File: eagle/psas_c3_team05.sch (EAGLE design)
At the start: 92 parts, among them IC1 CP2102, J1 3220-10-0100-00, J2 1.27MM_HDR_2X12X1, U1 MIC5319 3.3V, U2 MCP73871, U3 MKW01Z128, X1 32 MHz

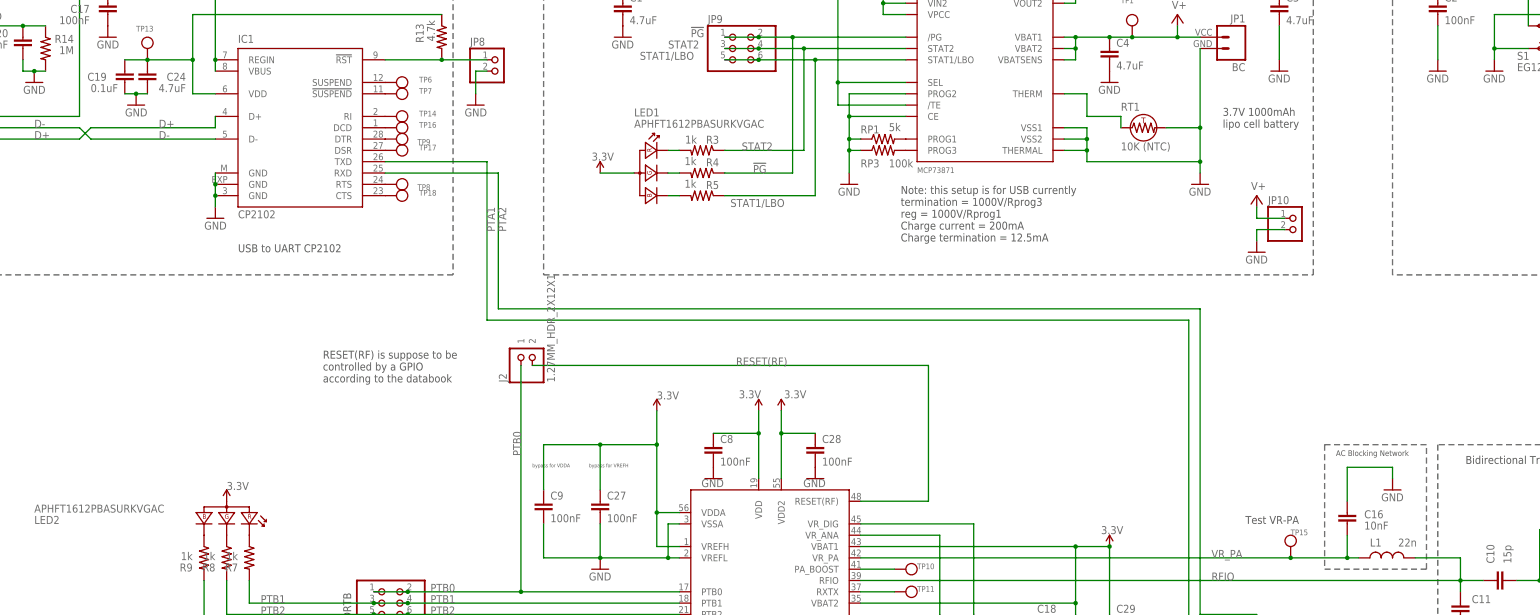
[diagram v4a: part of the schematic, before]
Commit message: I added a few more parts
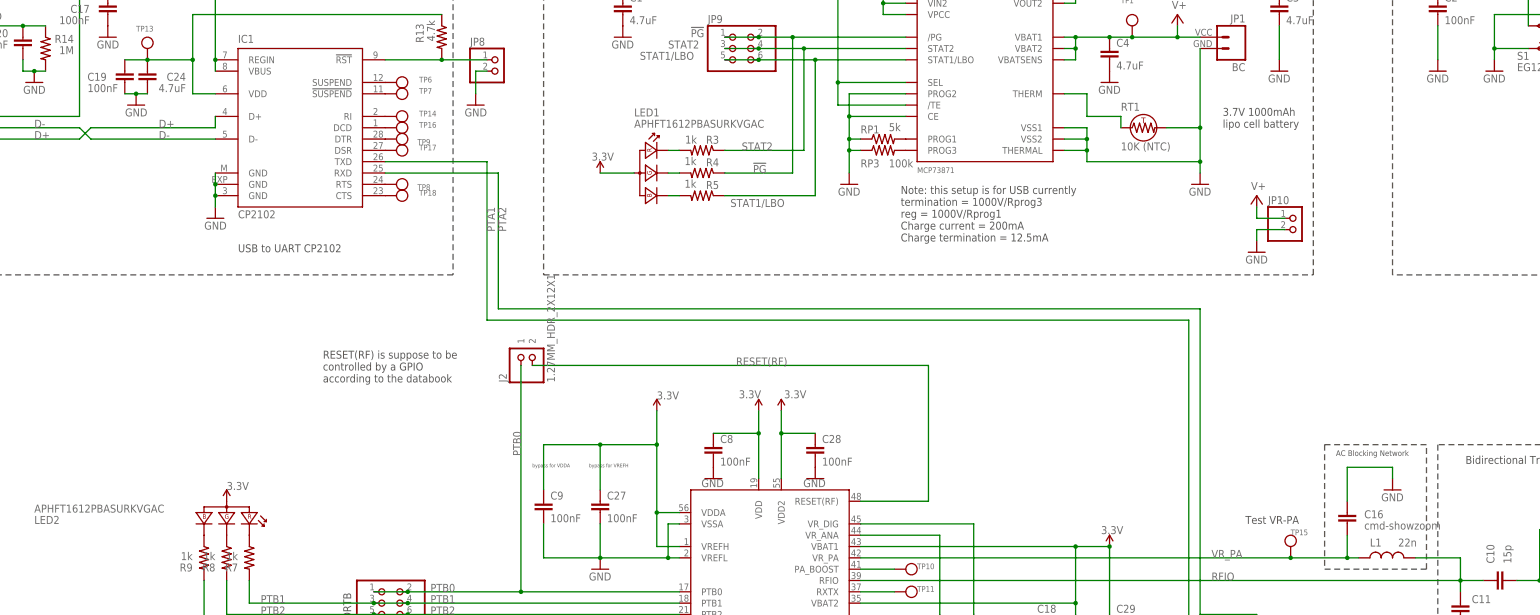
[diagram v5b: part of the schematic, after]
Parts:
- C15: DPN (none) -> 490-1532-1-ND
- C16: value 10nF -> cmd-showzoom
- C19: value 0.1uF -> 100nF
- C2, C5, C7: DPN (none) -> 490-1532-1-ND; DSN 490-1532-1-ND -> (none)
- C6: DPN (none) -> 490-3906-1-ND
- LED1, LED2: DPN 160-2022-1-ND -> 754-1100-1-ND
- LED3: DPN (none) -> 160-1446-1-ND
- R2: DPN (none) -> 311-1.00KHRCT-ND
- S1: DPN (none) -> EG1903-ND; DSN EG1903-ND -> (none)
- X1: DPN (none) -> SER3672CT-ND
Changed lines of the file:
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@@
 <part name="TP1" library="microbuilder" deviceset="TESTPOINT" device="ROUND0.5MM"/>
 <part name="C2" library="rcl_custom" deviceset="C-EU" device="0603-B-NOSILK" value="100nF">
-<attribute name="DSN" value="490-1532-1-ND"/>
+<attribute name="DPN" value="490-1532-1-ND"/>
 </part>
 <part name="GND4" library="Vibrogait_prototype" deviceset="GND" device=""/>
@@
 <part name="TP3" library="microbuilder" deviceset="TESTPOINT" device="ROUND0.5MM"/>
 <part name="C5" library="rcl_custom" deviceset="C-EU" device="0603-B-NOSILK" value="100nF">
-<attribute name="DSN" value="490-1532-1-ND"/>
-</part>
-<part name="C6" library="rcl_custom" deviceset="C-EU" device="0805-B-NOSILK" value="2.2uF"/>
+<attribute name="DPN" value="490-1532-1-ND"/>
+</part>
+<part name="C6" library="rcl_custom" deviceset="C-EU" device="0805-B-NOSILK" value="2.2uF">
+<attribute name="DPN" value="490-3906-1-ND"/>
+</part>
 <part name="C7" library="rcl_custom" deviceset="C-EU" device="0603-B-NOSILK" value="100nF">
-<attribute name="DSN" value="490-1532-1-ND"/>
+<attribute name="DPN" value="490-1532-1-ND"/>
 </part>
 <part name="GND7" library="Vibrogait_prototype" deviceset="GND" device=""/>
@@
 <part name="GND10" library="Vibrogait_prototype" deviceset="GND" device=""/>
 <part name="S1" library="Vibrogait_prototype" deviceset="SWITCH-SPST" device="PTH" value="EG1218">
-<attribute name="DSN" value="EG1903-ND"/>
+<attribute name="DPN" value="EG1903-ND"/>
 </part>
 <part name="GND11" library="Vibrogait_prototype" deviceset="GND" device=""/>
@@
 <part name="GND18" library="Vibrogait_prototype" deviceset="GND" device=""/>
 <part name="GND19" library="Vibrogait_prototype" deviceset="GND" device=""/>
-<part name="C15" library="rcl_custom" deviceset="C-EU" device="0603-B-NOSILK" value="100nF"/>
-<part name="C16" library="rcl_custom" deviceset="C-EU" device="0603-B-NOSILK" value="10nF"/>
+<part name="C15" library="rcl_custom" deviceset="C-EU" device="0603-B-NOSILK" value="100nF">
+<attribute name="DPN" value="490-1532-1-ND"/>
+</part>
+<part name="C16" library="rcl_custom" deviceset="C-EU" device="0603-B-NOSILK" value="cmd-showzoom"/>
 <part name="GND20" library="Vibrogait_prototype" deviceset="GND" device=""/>
 <part name="L1" library="rcl_custom" deviceset="L-US" device="0603-B-NOSILK" value="22n"/>
@@
 <attribute name="DPN" value="490-1532-1-ND"/>
 </part>
-<part name="C19" library="rcl_custom" deviceset="C-EU" device="0603-B-NOSILK" value="0.1uF">
+<part name="C19" library="rcl_custom" deviceset="C-EU" device="0603-B-NOSILK" value="100nF">
 <attribute name="DIST" value="Digi-Key"/>
 <attribute name="DPN" value="490-1532-1-ND"/>
@@
 <part name="GND25" library="Vibrogait_prototype" deviceset="GND" device=""/>
 <part name="LED1" library="Vibrogait_prototype" deviceset="LED_RGB_COMMON_ANODE-*" device="1.6X1.26" value="APHFT1612PBASURKVGAC">
-<attribute name="DPN" value="160-2022-1-ND"/>
+<attribute name="DPN" value="754-1100-1-ND"/>
 </part>
 <part name="R3" library="rcl_custom" deviceset="R-US_" device="0603-B-NOSILK" value="1k">
@@
 <part name="C21" library="rcl_custom" deviceset="C-EU" device="0603-B-NOSILK" value="1nF"/>
 <part name="GND27" library="Vibrogait_prototype" deviceset="GND" device=""/>
-<part name="X1" library="crystal" deviceset="FC-12M" device="" value="32 MHz"/>
+<part name="X1" library="crystal" deviceset="FC-12M" device="" value="32 MHz">
+<attribute name="DPN" value="SER3672CT-ND"/>
+</part>
 <part name="R6" library="rcl_custom" deviceset="R-US_" device="0603-B-NOSILK" value="0"/>
 <part name="C22" library="Vibrogait_prototype" deviceset="C-EU" device="0603-B-NOSILK" value="11pF">
@@
 <part name="TP18" library="microbuilder" deviceset="TESTPOINT" device="ROUND0.5MM"/>
 <part name="LED2" library="Vibrogait_prototype" deviceset="LED_RGB_COMMON_ANODE-*" device="1.6X1.26" value="APHFT1612PBASURKVGAC">
-<attribute name="DPN" value="160-2022-1-ND"/>
-</part>
-<part name="LED3" library="Vibrogait_prototype" deviceset="LED" device="-0603" value="GRN"/>
-<part name="R2" library="rcl_custom" deviceset="R-US_" device="0603-B-NOSILK" value="1k"/>
+<attribute name="DPN" value="754-1100-1-ND"/>
+</part>
+<part name="LED3" library="Vibrogait_prototype" deviceset="LED" device="-0603" value="GRN">
+<attribute name="DPN" value="160-1446-1-ND"/>
+</part>
+<part name="R2" library="rcl_custom" deviceset="R-US_" device="0603-B-NOSILK" value="1k">
+<attribute name="DPN" value="311-1.00KHRCT-ND"/>
+</part>
 <part name="GND38" library="Vibrogait_prototype" deviceset="GND" device=""/>
 <part name="R7" library="rcl_custom" deviceset="R-US_" device="0603-B-NOSILK" value="1k"/>
@@
 <attribute name="NAME" x="392.684" y="348.361" size="1.778" layer="95"/>
 <attribute name="VALUE" x="392.684" y="343.281" size="1.778" layer="96"/>
-<attribute name="DSN" x="391.16" y="347.98" size="1.778" layer="96" display="off"/>
+<attribute name="DPN" x="391.16" y="347.98" size="1.778" layer="96" display="off"/>
 </instance>
 <instance part="GND4" gate="1" x="391.16" y="332.74" smashed="yes">
@@
 <attribute name="NAME" x="451.104" y="345.821" size="1.778" layer="95"/>
 <attribute name="VALUE" x="451.104" y="340.741" size="1.778" layer="96"/>
-<attribute name="DSN" x="449.58" y="345.44" size="1.778" layer="96" display="off"/>
+<attribute name="DPN" x="449.58" y="345.44" size="1.778" layer="96" display="off"/>
 </instance>
 <instance part="C6" gate="CE" x="464.82" y="345.44" smashed="yes">
 <attribute name="NAME" x="466.344" y="345.821" size="1.778" layer="95"/>
 <attribute name="VALUE" x="466.344" y="340.741" size="1.778" layer="96"/>
+<attribute name="DPN" x="464.82" y="345.44" size="1.778" layer="96" display="off"/>
 </instance>
 <instance part="C7" gate="CE" x="439.42" y="337.82" smashed="yes">
 <attribute name="NAME" x="440.944" y="338.201" size="1.778" layer="95"/>
 <attribute name="VALUE" x="440.944" y="333.121" size="1.778" layer="96"/>
-<attribute name="DSN" x="439.42" y="337.82" size="1.778" layer="96" display="off"/>
+<attribute name="DPN" x="439.42" y="337.82" size="1.778" layer="96" display="off"/>
 </instance>
 <instance part="GND7" gate="1" x="439.42" y="327.66" smashed="yes">
@@
 <attribute name="NAME" x="408.94" y="335.28" size="1.778" layer="95"/>
 <attribute name="VALUE" x="408.94" y="332.74" size="1.778" layer="96"/>
-<attribute name="DSN" x="416.56" y="340.36" size="1.778" layer="96" rot="R180" display="off"/>
+<attribute name="DPN" x="416.56" y="340.36" size="1.778" layer="96" rot="R180" display="off"/>
 </instance>
 <instance part="GND11" gate="1" x="317.5" y="330.2" smashed="yes">
@@
 <attribute name="NAME" x="461.899" y="219.964" size="1.778" layer="95" rot="R90"/>
 <attribute name="VALUE" x="466.979" y="219.964" size="1.778" layer="96" rot="R90"/>
+<attribute name="DPN" x="462.28" y="218.44" size="1.778" layer="96" rot="R90" display="off"/>
 </instance>
 <instance part="C16" gate="CE" x="370.84" y="233.68" smashed="yes">
@@
 <attribute name="NAME" x="327.66" y="187.96" size="1.778" layer="95"/>
 <attribute name="VALUE" x="324.2056" y="195.0466" size="1.778" layer="96"/>
+<attribute name="DPN" x="328.93" y="193.04" size="1.778" layer="96" rot="R180" display="off"/>
 </instance>
 <instance part="R6" gate="R" x="312.42" y="193.04" smashed="yes" rot="R180">
@@
 <attribute name="NAME" x="480.06" y="346.71" size="1.778" layer="95"/>
 <attribute name="VALUE" x="480.06" y="344.17" size="1.778" layer="96"/>
+<attribute name="DPN" x="477.52" y="345.44" size="1.778" layer="96" display="off"/>
 </instance>
 <instance part="R2" gate="R" x="477.52" y="337.82" smashed="yes" rot="R90">
 <attribute name="NAME" x="480.06" y="339.09" size="1.778" layer="95"/>
 <attribute name="VALUE" x="480.06" y="336.55" size="1.778" layer="96"/>
+<attribute name="DPN" x="477.52" y="337.82" size="1.778" layer="96" rot="R90" display="off"/>
 </instance>
 <instance part="GND38" gate="1" x="477.52" y="327.66" smashed="yes">

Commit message: 
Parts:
- R7, R8, R9: DPN (none) -> 311-1.00KHRCT-ND
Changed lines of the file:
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@@
 </part>
 <part name="GND38" library="Vibrogait_prototype" deviceset="GND" device=""/>
-<part name="R7" library="rcl_custom" deviceset="R-US_" device="0603-B-NOSILK" value="1k"/>
-<part name="R8" library="rcl_custom" deviceset="R-US_" device="0603-B-NOSILK" value="1k"/>
-<part name="R9" library="rcl_custom" deviceset="R-US_" device="0603-B-NOSILK" value="1k"/>
+<part name="R7" library="rcl_custom" deviceset="R-US_" device="0603-B-NOSILK" value="1k">
+<attribute name="DPN" value="311-1.00KHRCT-ND"/>
+</part>
+<part name="R8" library="rcl_custom" deviceset="R-US_" device="0603-B-NOSILK" value="1k">
+<attribute name="DPN" value="311-1.00KHRCT-ND"/>
+</part>
+<part name="R9" library="rcl_custom" deviceset="R-US_" device="0603-B-NOSILK" value="1k">
+<attribute name="DPN" value="311-1.00KHRCT-ND"/>
+</part>
 <part name="P+9" library="Vibrogait_prototype" deviceset="3.3V" device=""/>
 <part name="J1" library="apdm-ic-v2" deviceset="JTAG_ARM-10-*" device="50MIL" value="3220-10-0100-00">
@@
 <attribute name="NAME" x="121.92" y="222.25" size="1.778" layer="95" rot="R180"/>
 <attribute name="VALUE" x="121.92" y="224.79" size="1.778" layer="96" rot="R180"/>
+<attribute name="DPN" x="124.46" y="223.52" size="1.778" layer="96" rot="R270" display="off"/>
 </instance>
 <instance part="R8" gate="R" x="119.38" y="223.52" smashed="yes" rot="R270">
 <attribute name="NAME" x="116.84" y="222.25" size="1.778" layer="95" rot="R180"/>
 <attribute name="VALUE" x="116.84" y="224.79" size="1.778" layer="96" rot="R180"/>
+<attribute name="DPN" x="119.38" y="223.52" size="1.778" layer="96" rot="R270" display="off"/>
 </instance>
 <instance part="R9" gate="R" x="114.3" y="223.52" smashed="yes" rot="R270">
 <attribute name="NAME" x="111.76" y="222.25" size="1.778" layer="95" rot="R180"/>
 <attribute name="VALUE" x="111.76" y="224.79" size="1.778" layer="96" rot="R180"/>
+<attribute name="DPN" x="114.3" y="223.52" size="1.778" layer="96" rot="R270" display="off"/>
 </instance>
 <instance part="P+9" gate="G$1" x="119.38" y="236.22" smashed="yes">

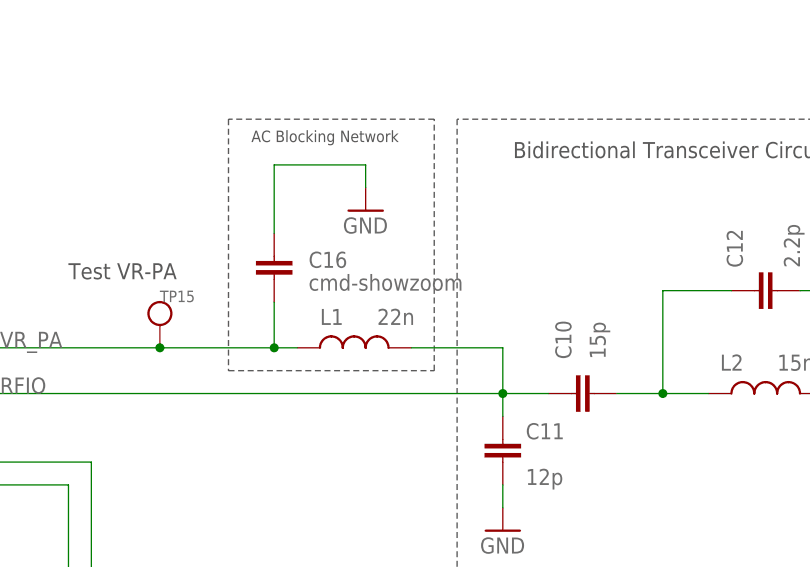
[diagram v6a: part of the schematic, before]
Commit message: 
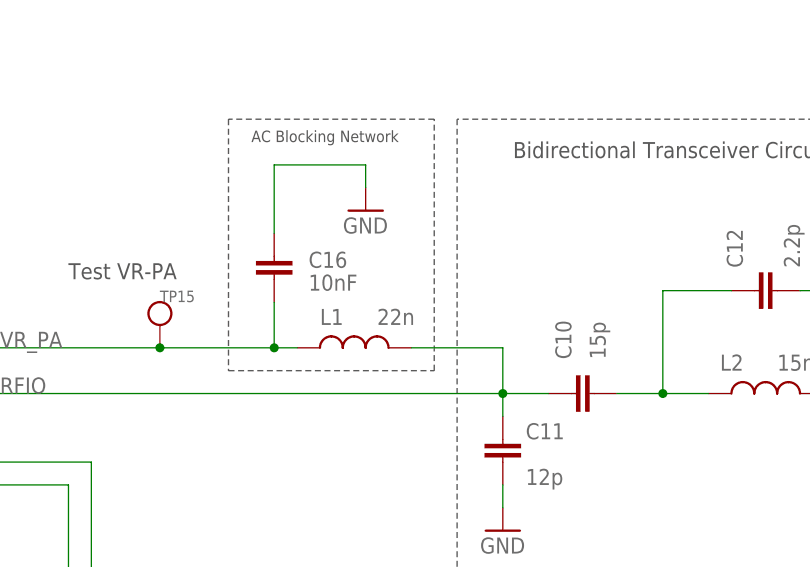
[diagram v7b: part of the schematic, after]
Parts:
- C16: value cmd-showzoom -> 10nF
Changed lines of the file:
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@@
 <attribute name="DPN" value="490-1532-1-ND"/>
 </part>
-<part name="C16" library="rcl_custom" deviceset="C-EU" device="0603-B-NOSILK" value="cmd-showzoom"/>
+<part name="C16" library="rcl_custom" deviceset="C-EU" device="0603-B-NOSILK" value="10nF"/>
 <part name="GND20" library="Vibrogait_prototype" deviceset="GND" device=""/>
 <part name="L1" library="rcl_custom" deviceset="L-US" device="0603-B-NOSILK" value="22n"/>

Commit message: added a bunch of part numbers
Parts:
- C1, C3, C4: DIST (none) -> Digi-Key; MFG (none) -> Wurth Electronics Inc; MFG-PN (none) -> 885012207025
- C17, C19, C20: MFG (none) -> Murata Electronics North America; MFG-PN (none) -> GRM188R71C104KA01D
- C2, C5, C7: DIST (none) -> Digi-Key; MFG (none) -> Murata Electronics North America; MFG-PN (none) -> GRM188R71C104KA01D
- C21: DIST (none) -> Digi-Key; DPN (none) -> 399-8984-1-ND; MFG (none) -> Kemet; MFG-PN (none) -> C0603C102K8RACTU
- C24: MFG (none) -> Wurth Electronics Inc; MFG-PN (none) -> 885012207025
- C6: DIST (none) -> Digi-Key; MFG (none) -> Murata Electronics North America; MFG-PN (none) -> GRM21BR71C225KA12L
- CF1: MFG (none) -> Hirose Electric Co Ltd; MFG-PN (none) -> ZX62D-B-5P8
- IC1: DIST (none) -> Digi-Key; DPN (none) -> 336-1160-1-ND; MFG (none) -> Silicon Labs; MFG-PN (none) -> CP2102-GMR
- J1: DIGIKEY-PN 1175-1627-ND -> (none); DIST (none) -> Digi-Key; DPN (none) -> 1175-1627-ND
- R1: DIST (none) -> Digi-Key; DPN (none) -> 311-10.0KHRCT-ND; MFG (none) -> Yageo; MFG-PN (none) -> RC0603FR-0710KL
- R13: DIST (none) -> Digi-Key; MFG (none) -> Yageo; MFG-PN (none) -> RC0603JR-074K7P
- R14: MFG (none) -> Yageo; MFG-PN (none) -> RC0603FR-071ML
- R2, R3, R4, R5, R7, R8, R9: DIST (none) -> Digi-Key; MFG (none) -> Yageo; MFG-PN (none) -> RC0603FR-071KL
- RP1: DIST (none) -> Digi-Key; MFG (none) -> Yageo; MFG-PN (none) -> RC0603FR-074K99P
- RP3: DIST (none) -> Digi-Key; MFG (none) -> Yageo; MFG-PN (none) -> RC0603FR-07100KL
- RT1: DIST (none) -> Digi-Key; MFG (none) -> Honeywell Sensing and Control; MFG-PN (none) -> 175-103LAE-301
- S1: DIST (none) -> Digi-Key; MFG (none) -> E-Switch; MFG-PN (none) -> EG1218
- S2: DIST (none) -> Digi-Key; DPN (none) -> 450-1759-1-ND; MFG (none) -> TE Connectivity Alcoswitch Switches; MFG-PN (none) -> FSM4JSMATR
- U2: DIST (none) -> Digi-Key; DPN (none) -> MCP73871-2CCI/ML-ND; MFG (none) -> Microchip Technology; MFG-PN (none) -> MCP73871-2CCI/ML
